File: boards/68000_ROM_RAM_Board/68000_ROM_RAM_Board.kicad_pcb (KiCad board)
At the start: 2 copper layers, 101.6 x 55.9 mm, 16 parts, among them J1 Conn_01x32, M1 RC2014_40_PIN, U1 74LS125, U3 W27C512, U4 AS6C4008-55PCN, U5 AS6C4008-55PCN, U6 W27C512, U8 74LS138, U9 74LS139

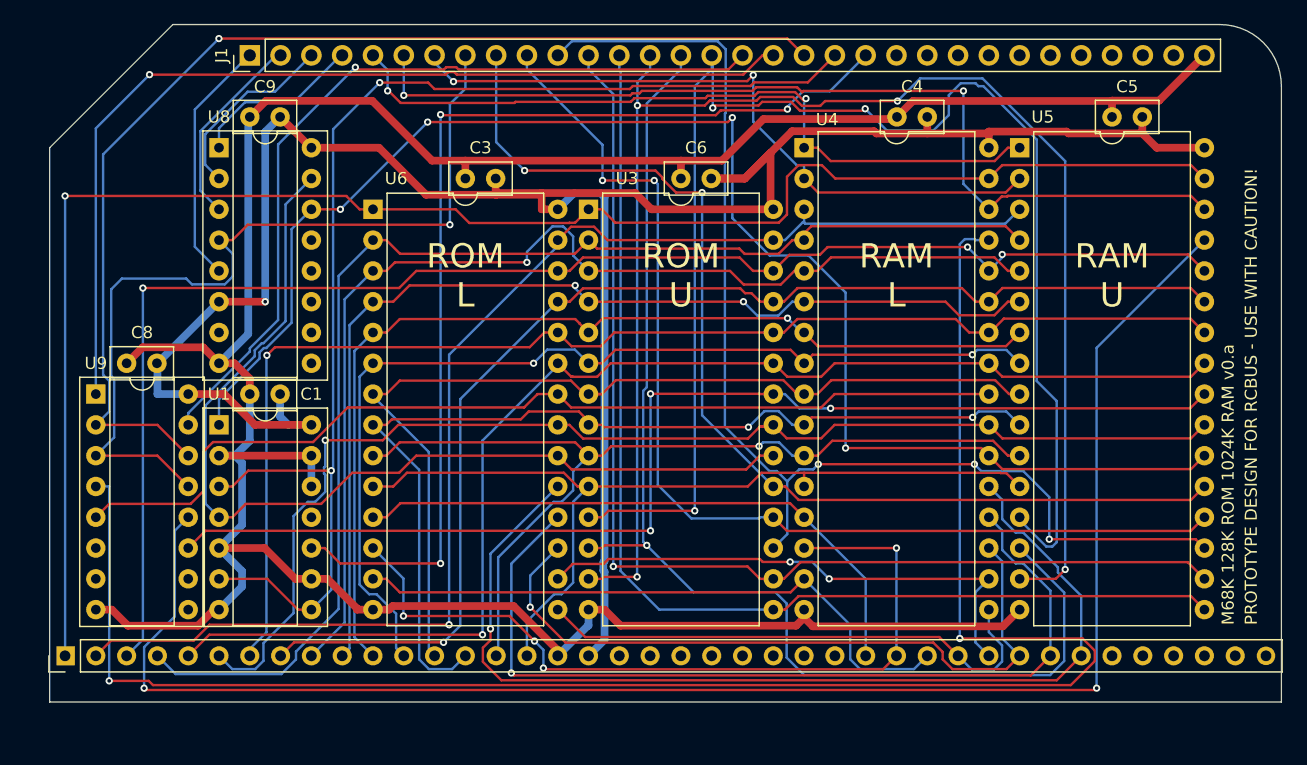
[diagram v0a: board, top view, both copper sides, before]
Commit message: Update to v2 board set
Lots of updates to reflect the new v2 boards that use the full RCBus 80 pins as well as slight modifications to the various test programs to reflect the new IO and MEM space addresses.
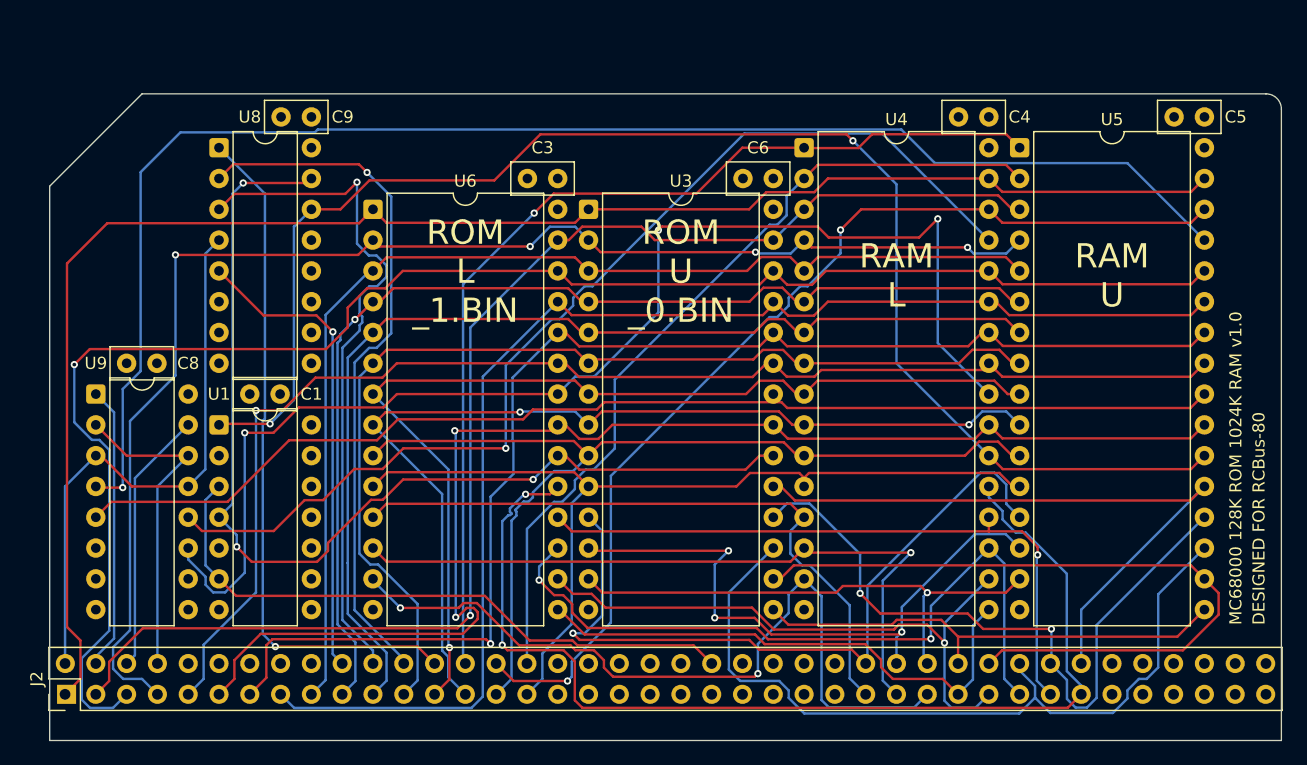
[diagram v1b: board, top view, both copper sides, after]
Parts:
- removed J1: Conn_01x32, Connector_PinHeader_2.54mm:PinHeader_1x32_P2.54mm_Vertical
- removed M1: RC2014_40_PIN, MyLibrary2023:RC2014_STD_40_PIN
- added J2: RCBus_80PIN_68000, MyLibrary2023:RCBus_80p_Medium, F.Cu at (85.1, 111.8)
- U1: footprint Package_DIP:DIP-14_W7.62mm_Socket -> Package_DIP:DIP-14_W7.62mm
- U8, U9: footprint Package_DIP:DIP-16_W7.62mm_Socket -> Package_DIP:DIP-16_W7.62mm
- moved C3 5.12 mm to (127.0, 65.4)
- moved C5 5.12 mm to (177.8, 60.3)
- moved C6 5.12 mm to (144.8, 65.4)
- moved C4 5.08 mm to (160.1, 60.3)
- moved C9 2.58 mm to (104.2, 60.3)
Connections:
- U1 pad 10: /~{RCBUS_DTACK} -> GND
- U1 pad 8: /~{DTACK} -> unconnected-(U1-Pad8)
- U9 pad 1: /~{LDS} -> /~{UDS}
- U9 pad 11: /~{RD_HI} -> /~{RD_LO}
- U9 pad 12: /~{WR_HI} -> /~{WR_LO}
- U9 pad 15: /~{UDS} -> /~{LDS}
- U9 pad 4: /~{WR_LO} -> /~{WR_HI}
- U9 pad 5: /~{RD_LO} -> /~{RD_HI}
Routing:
- net GND: track 241.0 -> 0.00 mm
- net +5V: track 199.0 -> 0.00 mm, vias 1 -> 0
- net /~{RCBUS_DTACK}: track 85.4 -> 0.00 mm, vias 3 -> 0
- net /D10: track 124.9 -> 42.6 mm, vias 4 -> 1
- net /R/~{W}: track 94.0 -> 26.9 mm, vias 1 -> 0
- net /D8: track 120.8 -> 61.9 mm, vias 3 -> 1
- net /~{WR_LO}: track 146.9 -> 88.2 mm, vias 2 -> 1
- net /~{LDS}: track 80.5 -> 21.8 mm, vias 1 -> 0
- net /D11: track 93.0 -> 40.0 mm
- net /~{DTACK}: track 103.2 -> 52.1 mm, vias 2 -> 0
- net /D9: track 99.5 -> 50.9 mm, vias 1 -> 3
- net /~{UDS}: track 67.9 -> 22.9 mm, vias 1 -> 0
- net /A20: track 14.1 -> 56.9 mm, vias 0 -> 1
- net /A21: track 15.6 -> 57.3 mm, vias 0 -> 1
- net /A22: track 15.9 -> 56.5 mm, vias 0 -> 1
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- added copper zone on In1.Cu, net +5V
- added copper zone on In2.Cu, net GND
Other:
- board size 101.6 x 55.9 mm -> 101.6 x 53.3 mm
- copper layers 2 -> 4
- board text added: "DESIGNED FOR RCBus-80"
- board text added: "JLCJLCJLCJLC"
- board text added: "MC68000 128K ROM 1024K RAM v1.0"
- board text added: "ROM L _1.BIN"
- board text added: "ROM LOWER BYTE EASYBIN *_1.BIN FILE"
- board text added: "ROM U _0.BIN"
- board text added: "ROM UPPER BYTE EASYBIN *_0.BIN FILE"
- board text removed: "M68K 128K ROM 1024K RAM v0.a"
- board text removed: "PROTOTYPE DESIGN FOR RCBUS - USE WITH CAUTION!"
- board text removed: "ROM L"
- board text removed: "ROM LOWER BYTE"
- board text removed: "ROM U"
- board text removed: "ROM UPPER BYTE"
